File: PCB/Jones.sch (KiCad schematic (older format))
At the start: 248 parts, among them J1 USB_C_Receptacle_USB2.0, J2 Conn_01x03, J3 Conn_01x02, J5 Conn_02x03_Odd_Even, U1 ATmega32U4-MU, U2 24LC64, Y1 16MHz

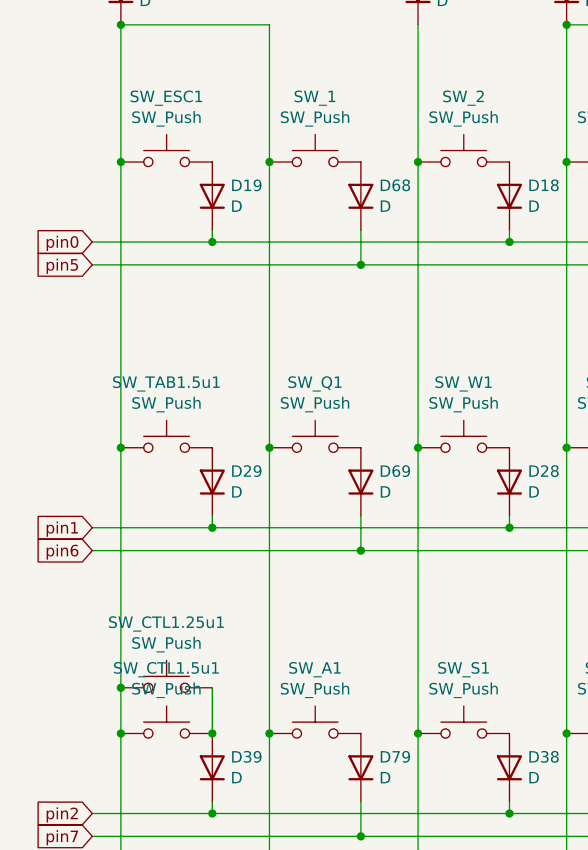
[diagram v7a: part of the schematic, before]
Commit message: 40s用、R2のTABに、1u、1.25uを追加
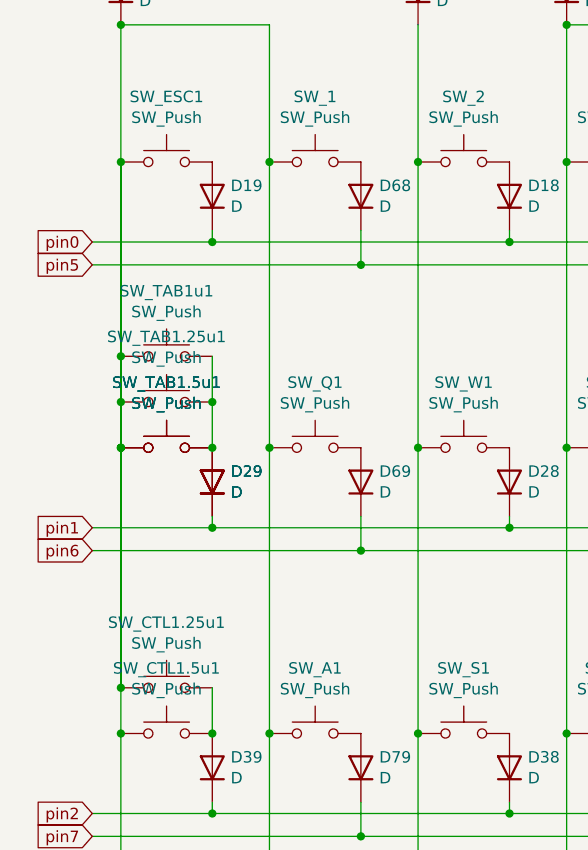
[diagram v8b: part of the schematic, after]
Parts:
- added SW_TAB1.25u1: SW_Push, MX_Alps_Hybrid:MXOnly-1.25U-Hotswap-guide-Rotate, symbol Switch:SW_Push
- added SW_TAB1u1: SW_Push, MX_Alps_Hybrid:MXOnly-1U-Hotswap-guide-4pin, symbol Switch:SW_Push
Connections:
- net RE2_1: now also SW_TAB1.25u1.1, SW_TAB1u1.1
- net at D29.2 (A), SW_TAB1.5u1.2: now also SW_TAB1.25u1.2, SW_TAB1u1.2
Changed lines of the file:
@@
 Wire Wire Line
 	14725 1575 14825 1575
+Wire Wire Line
+	925  2075 925  2925
+Wire Wire Line
+	925  3325 925  4375
+Connection ~ 925  3325
+$Comp
+L Switch:SW_Push SW_TAB1.5u1
+U 1 1 5F65B333
+P 1125 3325
+F 0 "SW_TAB1.5u1" H 1125 3610 50  0000 C CNN
+F 1 "SW_Push" H 1125 3519 50  0000 C CNN
+F 2 "MX_Alps_Hybrid:MXOnly-1.5U-Hotswap-guide" H 1125 3525 50  0001 C CNN
+F 3 "~" H 1125 3525 50  0001 C CNN
+	1    1125 3325
+	1    0    0    -1
+$EndComp
+$Comp
+L Device:D D29
+U 1 1 5F65B339
+P 1325 3475
+F 0 "D29" V 1371 3395 50  0000 R CNN
+F 1 "D" V 1280 3395 50  0000 R CNN
+F 2 "Diode_SMD:D_SOD-123" H 1325 3475 50  0001 C CNN
+F 3 "~" H 1325 3475 50  0001 C CNN
+F 4 "C81598" H 1325 3475 50  0001 C CNN "LCSC"
+	1    1325 3475
+	0    -1   -1   0
+$EndComp
+$Comp
+L Switch:SW_Push SW_TAB1.25u1
+U 1 1 615879B4
+P 1125 3125
+F 0 "SW_TAB1.25u1" H 1125 3410 50  0000 C CNN
+F 1 "SW_Push" H 1125 3319 50  0000 C CNN
+F 2 "MX_Alps_Hybrid:MXOnly-1.25U-Hotswap-guide-Rotate" H 1125 3325 50  0001 C CNN
+F 3 "~" H 1125 3325 50  0001 C CNN
+	1    1125 3125
+	1    0    0    -1
+$EndComp
+$Comp
+L Switch:SW_Push SW_TAB1u1
+U 1 1 615B818E
+P 1125 2925
+F 0 "SW_TAB1u1" H 1125 3210 50  0000 C CNN
+F 1 "SW_Push" H 1125 3119 50  0000 C CNN
+F 2 "MX_Alps_Hybrid:MXOnly-1U-Hotswap-guide-4pin" H 1125 3125 50  0001 C CNN
+F 3 "~" H 1125 3125 50  0001 C CNN
+	1    1125 2925
+	1    0    0    -1
+$EndComp
+Connection ~ 925  2925
+Wire Wire Line
+	925  2925 925  3125
+Connection ~ 925  3125
+Wire Wire Line
+	925  3125 925  3325
+Wire Wire Line
+	1325 2925 1325 3125
+Connection ~ 1325 3325
+Connection ~ 1325 3125
+Wire Wire Line
+	1325 3125 1325 3325
 $EndSCHEMATC
